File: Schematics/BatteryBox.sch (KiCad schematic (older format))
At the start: 1 part, among them P2 Conn_WallPlug

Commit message: finalize schematic
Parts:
- removed P2: Conn_WallPlug, symbol Connector:Conn_WallPlug
- added X1: 12VKfz_Plug, symbol MyParts:12VKfz_Plug
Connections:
- new net CoolerBox2/12V_In_MainBattery: X1.12V
- new net CoolerBox2/GND_In_MainBattery: X1.GND
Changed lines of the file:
@@
 $EndDescr
 $Sheet
-S 8350 1450 1400 2350
+S 9350 3750 1400 2350
 U 5EF099A0
 F0 "CoolerBox" 50
 F1 "CoolerBox.sch" 50
-F2 "V_DC" I L 8350 2000 50
-F3 "GND" I L 8350 2300 50
-F4 "AC_P" I L 8350 2700 50
-F5 "AC_N" I L 8350 3000 50
+F2 "V_DC" I L 9350 4300 50
+F3 "GND" I L 9350 4600 50
+F4 "AC_P" I L 9350 5000 50
+F5 "AC_N" I L 9350 5200 50
 $EndSheet
 $Sheet
-S 3000 1750 1500 3500
+S 7500 3750 1500 3500
 U 5EF0A72F
 F0 "BatteryBoxEuro" 50
 F1 "BatteryBoxEuro.sch" 50
-F2 "OUT1_12V" I R 4500 2000 50
-F3 "OUT1_GND" I R 4500 2300 50
+F2 "OUT1_12V" I R 9000 4000 50
+F3 "OUT1_GND" I R 9000 4300 50
 $EndSheet
-Wire Wire Line
-	4500 2000 8350 2000
-Wire Wire Line
-	4500 2300 8350 2300
-$Comp
-L Connector:Conn_WallPlug P2
-U 1 1 5EF0BCF3
-P 6600 2800
-F 0 "P2" H 6617 3125 50  0000 C CNN
-F 1 "Conn_WallPlug" H 6617 3034 50  0000 C CNN
-F 2 "" H 7000 2800 50  0001 C CNN
-F 3 "~" H 7000 2800 50  0001 C CNN
-	1    6600 2800
-	1    0    0    -1
-$EndComp
-Wire Wire Line
-	6800 2700 8350 2700
-Wire Wire Line
-	6800 2900 7550 2900
-Wire Wire Line
-	7550 2900 7550 3000
-Wire Wire Line
-	7550 3000 8350 3000
 $Sheet
-S 5650 4600 1050 1650
+S 7850 950  1050 1650
 U 5F0C81D9
 F0 "BatteryPowerBox" 50
 F1 "BatteryPowerBox.sch" 50
-F2 "L_IN" I L 5650 4800 50
-F3 "N_IN" I L 5650 5000 50
-F4 "12V+_OUT" I L 5650 5750 50
-F5 "0V_OUT" I L 5650 5950 50
-F6 "PE" I L 5650 5200 50
+F2 "L_IN" I L 7850 1150 50
+F3 "N_IN" I L 7850 1350 50
+F4 "12V+_OUT" I L 7850 2050 50
+F5 "0V_OUT" I L 7850 2300 50
+F6 "PE" I L 7850 1550 50
 $EndSheet
+Wire Wire Line
+	4800 2300 7850 2300
 $Sheet
-S 4150 6800 1600 400
+S 2600 950  2200 2500
 U 5F0EC429
 F0 "CoolerBox2" 50
 F1 "CoolerBox2.sch" 50
+F2 "12V_In_MainBattery" I L 2600 1350 50
+F3 "GND_In_MainBattery" I L 2600 1500 50
+F4 "12V_In_SecBattery" I R 4800 2050 50
+F5 "GND_In_SecBattery" I R 4800 2300 50
+F6 "230V_L" I R 4800 1150 50
+F7 "230V_N" I R 4800 1350 50
+F8 "PE" I R 4800 1550 50
 $EndSheet
+Wire Wire Line
+	4800 2050 7850 2050
+Wire Wire Line
+	4800 1150 7850 1150
+Wire Wire Line
+	4800 1350 7850 1350
+Wire Wire Line
+	4800 1550 7850 1550
+$Comp
+L MyParts:12VKfz_Plug X1
+U 1 1 5F0D9E08
+P 1350 1200
+F 0 "X1" H 1442 1315 50  0000 C CNN
+F 1 "12VKfz_Plug" H 1442 1224 50  0000 C CNN
+F 2 "" H 1350 1200 50  0001 C CNN
+F 3 "" H 1350 1200 50  0001 C CNN
+	1    1350 1200
+	-1   0    0    -1
+$EndComp
+Wire Wire Line
+	1800 1350 2600 1350
+Wire Wire Line
+	1800 1500 2600 1500
 $EndSCHEMATC

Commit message: some modifications
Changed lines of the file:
@@
 $Descr A4 11693 8268
 encoding utf-8
-Sheet 1 6
+Sheet 1 4
 Title ""
 Date ""
@@
 $EndDescr
 $Sheet
-S 9350 3750 1400 2350
-U 5EF099A0
-F0 "CoolerBox" 50
-F1 "CoolerBox.sch" 50
-F2 "V_DC" I L 9350 4300 50
-F3 "GND" I L 9350 4600 50
-F4 "AC_P" I L 9350 5000 50
-F5 "AC_N" I L 9350 5200 50
-$EndSheet
-$Sheet
-S 7500 3750 1500 3500
-U 5EF0A72F
-F0 "BatteryBoxEuro" 50
-F1 "BatteryBoxEuro.sch" 50
-F2 "OUT1_12V" I R 9000 4000 50
-F3 "OUT1_GND" I R 9000 4300 50
-$EndSheet
-$Sheet
 S 7850 950  1050 1650

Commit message: Version 3
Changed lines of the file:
@@
 $Descr A4 11693 8268
 encoding utf-8
-Sheet 1 4
+Sheet 1 5
 Title ""
 Date ""
@@
 Wire Wire Line
 	1800 1500 2600 1500
+$Sheet
+S 4000 4350 2150 1600
+U 60AB0555
+F0 "Sheet60AB0554" 50
+F1 "12V_PowerSelection.sch" 50
+$EndSheet
 $EndSCHEMATC

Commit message: work on EoroBox
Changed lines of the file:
@@
 $Descr A4 11693 8268
 encoding utf-8
-Sheet 1 5
+Sheet 1 9
 Title ""
 Date ""
@@
 	1800 1500 2600 1500
 $Sheet
-S 4000 4350 2150 1600
-U 60AB0555
-F0 "Sheet60AB0554" 50
-F1 "12V_PowerSelection.sch" 50
+S 2600 4050 2200 2850
+U 60D529AB
+F0 "EuroPowerBox" 50
+F1 "EuroPowerBox.sch" 50
 $EndSheet
+Text HLabel 2600 4400 0    50   Input ~ 0
+12V_In_Main
 $EndSCHEMATC

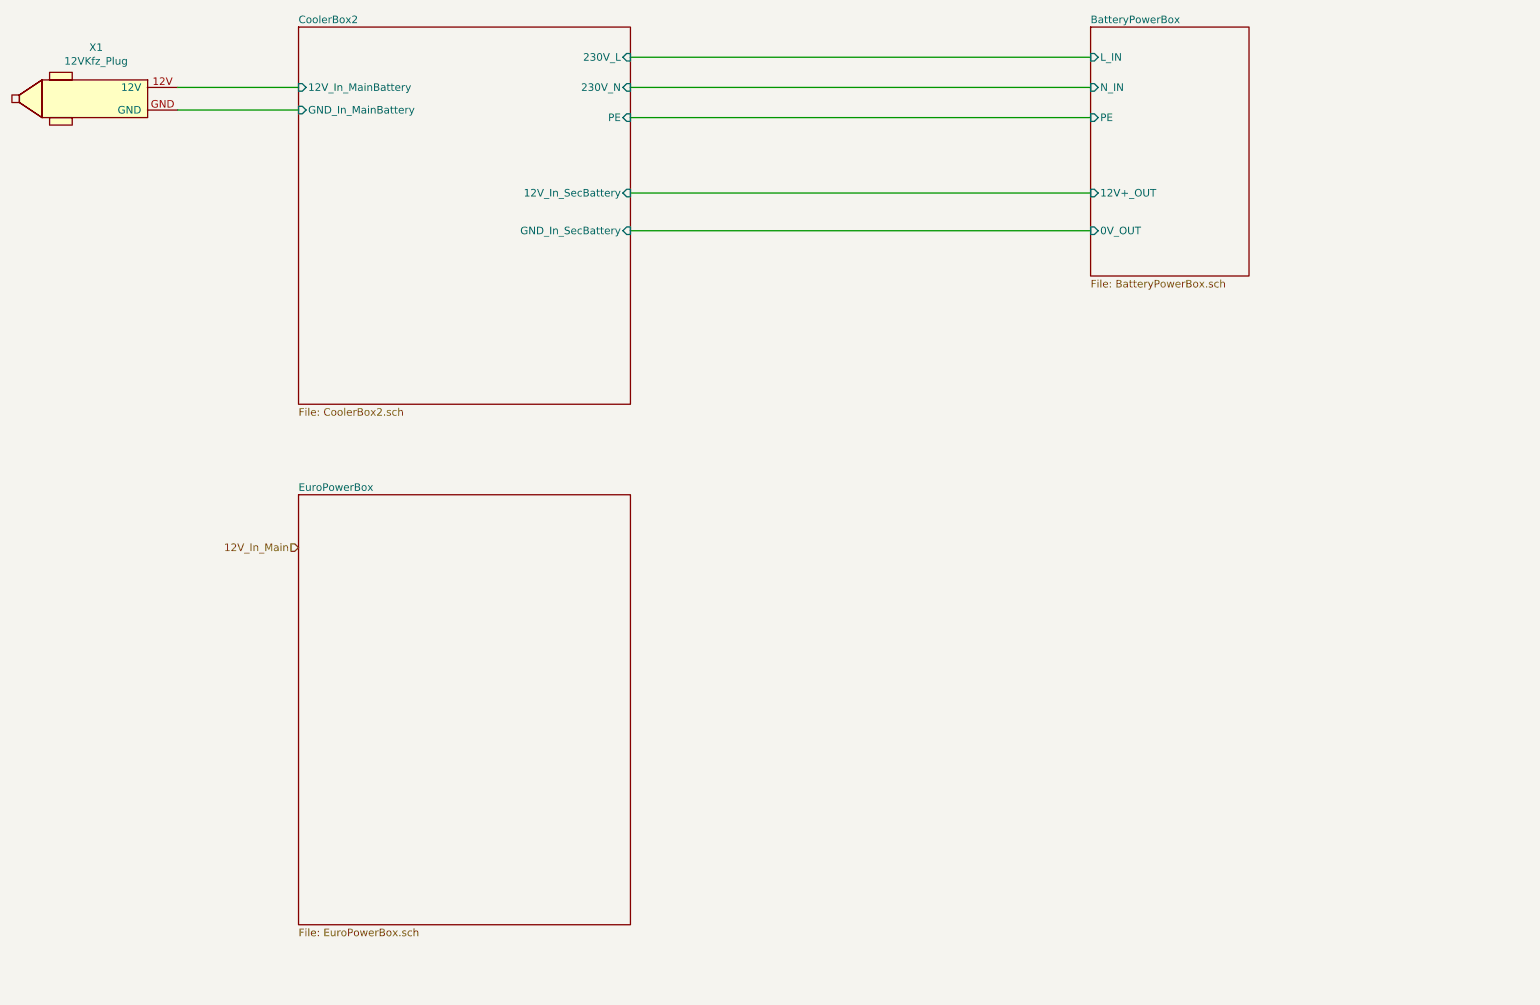
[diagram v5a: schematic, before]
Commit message: delete old schematic
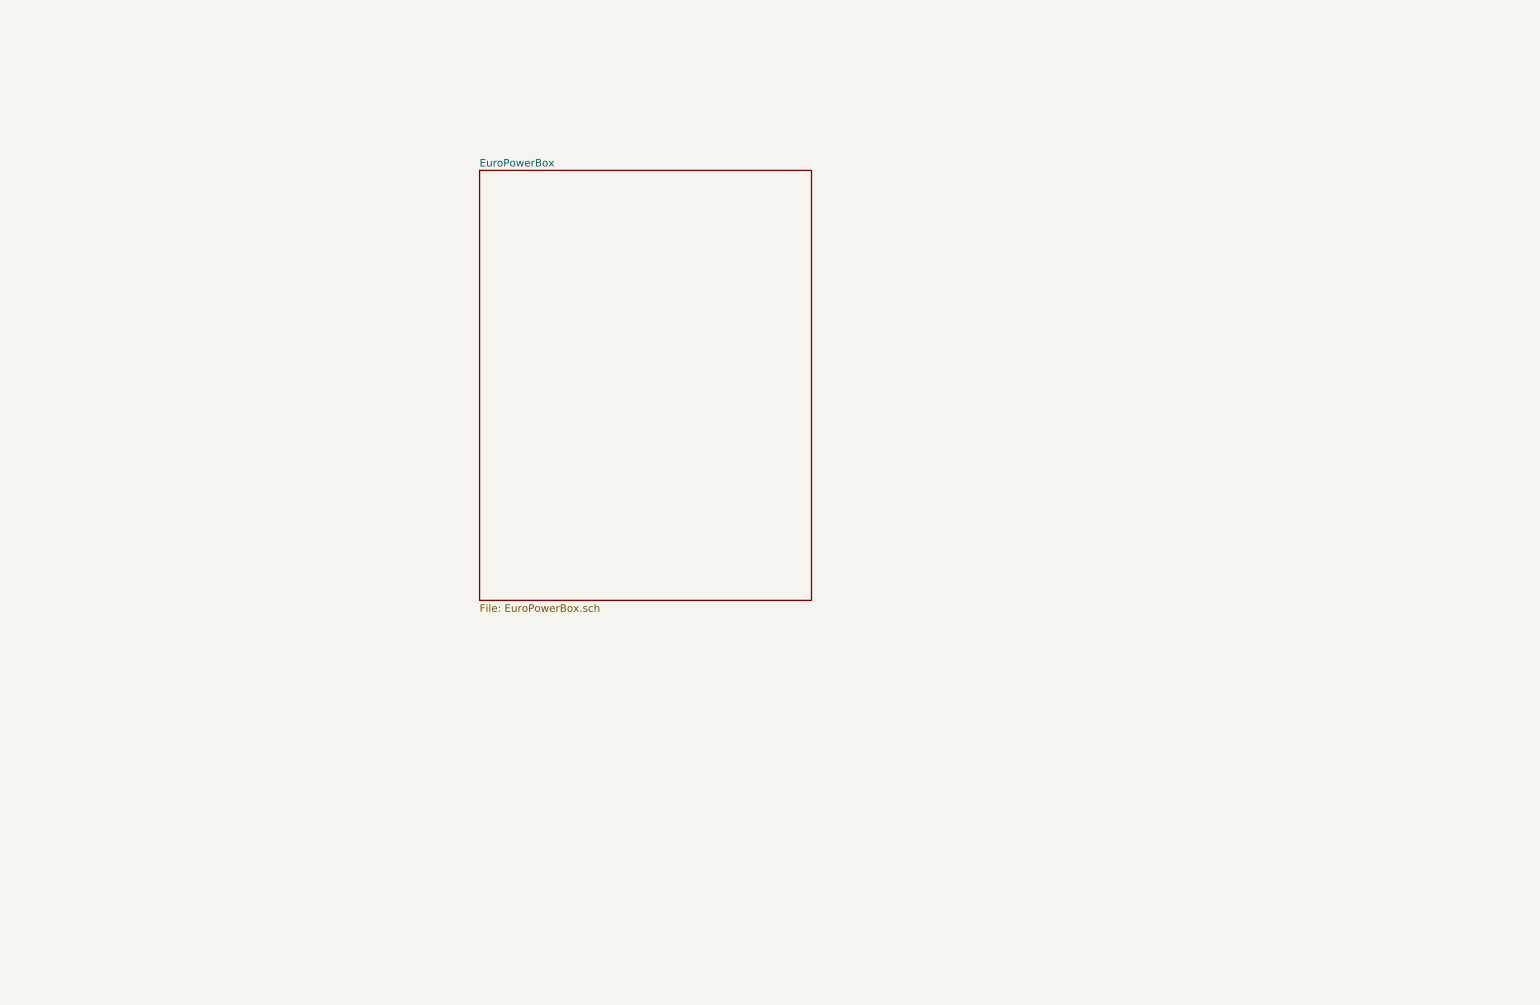
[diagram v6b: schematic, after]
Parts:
- removed X1: 12VKfz_Plug, symbol MyParts:12VKfz_Plug
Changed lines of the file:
@@
 $Descr A4 11693 8268
 encoding utf-8
-Sheet 1 9
+Sheet 1 6
 Title ""
 Date ""
@@
 $EndDescr
 $Sheet
-S 7850 950  1050 1650
-U 5F0C81D9
-F0 "BatteryPowerBox" 50
-F1 "BatteryPowerBox.sch" 50
-F2 "L_IN" I L 7850 1150 50
-F3 "N_IN" I L 7850 1350 50
-F4 "12V+_OUT" I L 7850 2050 50
-F5 "0V_OUT" I L 7850 2300 50
-F6 "PE" I L 7850 1550 50
-$EndSheet
-Wire Wire Line
-	4800 2300 7850 2300
-$Sheet
-S 2600 950  2200 2500
-U 5F0EC429
-F0 "CoolerBox2" 50
-F1 "CoolerBox2.sch" 50
-F2 "12V_In_MainBattery" I L 2600 1350 50
-F3 "GND_In_MainBattery" I L 2600 1500 50
-F4 "12V_In_SecBattery" I R 4800 2050 50
-F5 "GND_In_SecBattery" I R 4800 2300 50
-F6 "230V_L" I R 4800 1150 50
-F7 "230V_N" I R 4800 1350 50
-F8 "PE" I R 4800 1550 50
-$EndSheet
-Wire Wire Line
-	4800 2050 7850 2050
-Wire Wire Line
-	4800 1150 7850 1150
-Wire Wire Line
-	4800 1350 7850 1350
-Wire Wire Line
-	4800 1550 7850 1550
-$Comp
-L MyParts:12VKfz_Plug X1
-U 1 1 5F0D9E08
-P 1350 1200
-F 0 "X1" H 1442 1315 50  0000 C CNN
-F 1 "12VKfz_Plug" H 1442 1224 50  0000 C CNN
-F 2 "" H 1350 1200 50  0001 C CNN
-F 3 "" H 1350 1200 50  0001 C CNN
-	1    1350 1200
-	-1   0    0    -1
-$EndComp
-Wire Wire Line
-	1800 1350 2600 1350
-Wire Wire Line
-	1800 1500 2600 1500
-$Sheet
-S 2600 4050 2200 2850
+S 3800 1900 2200 2850
 U 60D529AB
 F0 "EuroPowerBox" 50
 F1 "EuroPowerBox.sch" 50
 $EndSheet
-Text HLabel 2600 4400 0    50   Input ~ 0
-12V_In_Main
 $EndSCHEMATC
